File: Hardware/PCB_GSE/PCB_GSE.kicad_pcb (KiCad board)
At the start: 2 copper layers, 139 parts, among them J1 Conn_01x06_Pin, J2 Vin_XT30PW-F, J3 Screw_Terminal_01x06, J4 GT17HN-4DP-2H(D)(56), J5 Conn_02x10_Top_Bottom, J6 Conn_01x02, J7 Screw_Terminal_01x04, J8 Screw_Terminal_01x04, U1 STM32F103CBT6, U10 INA125UA/2K5, U11 MAX6612MXK, U2 LM2673SX-12_NOPB, U3 MPQ9843GLE-5-AEC1-Z, U4 TLV75733PDBVR, U5 SI5442DU-T1-GE3, U6 SI5442DU-T1-GE3, U7 SI5442DU-T1-GE3, U8 ISOW1044, U9 INA125UA/2K5

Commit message: feat: add 8MHz crystal, fix extended ios, fix pinout with HSE, update smt32 project, begin layout edge
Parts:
- added C54: 22pF, Capacitor_SMD:C_0805_2012Metric, F.Cu at (141.7, 49.2)
- added C55: 22pF, Capacitor_SMD:C_0805_2012Metric, F.Cu at (141.7, 52.2)
- added R42: 10R, Resistor_SMD:R_0805_2012Metric, F.Cu at (146.2, 49.1)
- added XTAL-1: 830050510, PCB_GSE:830050510, F.Cu at (147.6, 44.4)
- J5: value Conn_02x10_Top_Bottom -> Conn_02x09_Top_Bottom; footprint Connector_PinHeader_2.54mm:PinHeader_2x10_P2.54mm_Vertical -> Connector_PinHeader_2.54mm:PinHeader_2x09_P2.54mm_Vertical
- moved C13 130.5 mm to (211.3, 34.4)
- moved C20 130.5 mm to (211.3, 41.9)
- moved C22 130.5 mm to (217.4, 30.8)
- moved C23 130.5 mm to (269.4, 23.3)
- moved C26 130.5 mm to (211.3, 38.1)
- moved C28 130.5 mm to (269.4, 29.3)
- moved C31 130.5 mm to (269.4, 32.3)
- moved C33 130.5 mm to (218.1, 63.7)
- moved C39 130.5 mm to (257.5, 54.4)
- moved C40 130.5 mm to (257.5, 57.4)
- moved C42 130.5 mm to (257.5, 60.4)
- moved C44 130.5 mm to (261.9, 54.4)
- moved C46 130.5 mm to (261.9, 57.4)
- moved C47 130.5 mm to (261.9, 60.4)
- moved C48 130.5 mm to (349.9, 54.2)
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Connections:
- J5 pad 10: LC_IN- -> 12V_Main
- J5 pad 11: 12V_Main -> EXTEND_IO6
- J5 pad 18: EXTEND_IO13 -> LC_IN-
- J5 pad 8: EXTEND_IO6 -> LC_IN-
- R4 pad 2: Net-(U1-PD0) -> Net-(U1-PC14)
- R5 pad 2: Net-(U1-PD1) -> Net-(U1-PC15)
- U1 pad 18: EXTEND_IO3 -> EXTEND_IO1
- U1 pad 19: EXTEND_IO4 -> EXTEND_IO2
- U1 pad 20: EXTEND_IO5 -> EXTEND_IO3
- U1 pad 25: EXTEND_IO6 -> EXTEND_IO4
- U1 pad 26: EXTEND_IO7 -> EXTEND_IO5
- U1 pad 27: EXTEND_IO8 -> EXTEND_IO6
- U1 pad 28: EXTEND_IO9 -> EXTEND_IO7
- U1 pad 29: EXTEND_IO10 -> EXTEND_IO8
- U1 pad 3: EXTEND_IO1 -> Net-(U1-PC14)
- U1 pad 30: EXTEND_IO11 -> EXTEND_IO9
- U1 pad 38: EXTEND_IO12 -> EXTEND_IO10
- U1 pad 4: EXTEND_IO2 -> Net-(U1-PC15)
- U1 pad 40: EXTEND_IO13 -> EXTEND_IO11
- U1 pad 41: EXTEND_IO14 -> EXTEND_IO12
- U1 pad 5: Net-(U1-PD0) -> OSC_IN
- U1 pad 6: Net-(U1-PD1) -> OSC_OUT
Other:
- board outline added: 76.2 x 101.6 mm

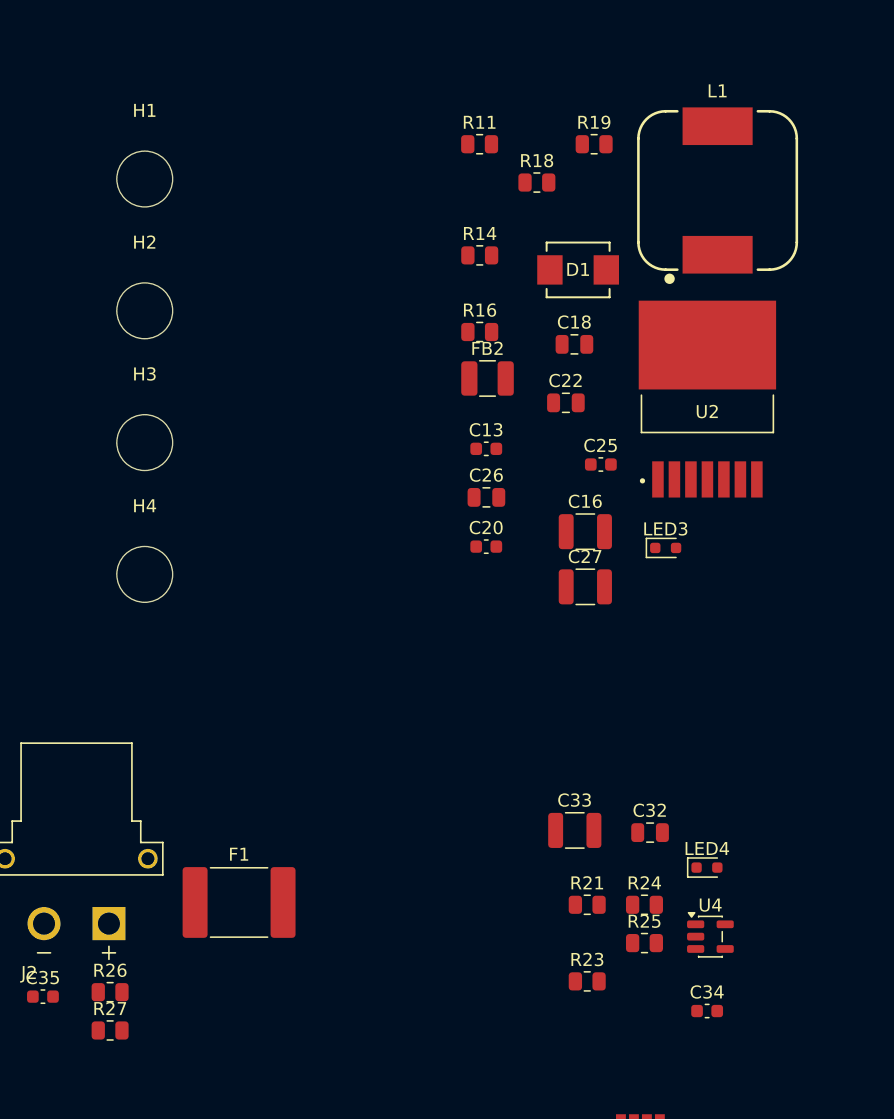
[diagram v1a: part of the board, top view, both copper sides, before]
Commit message: fix(GSE & Moteur): change Vin adc divider
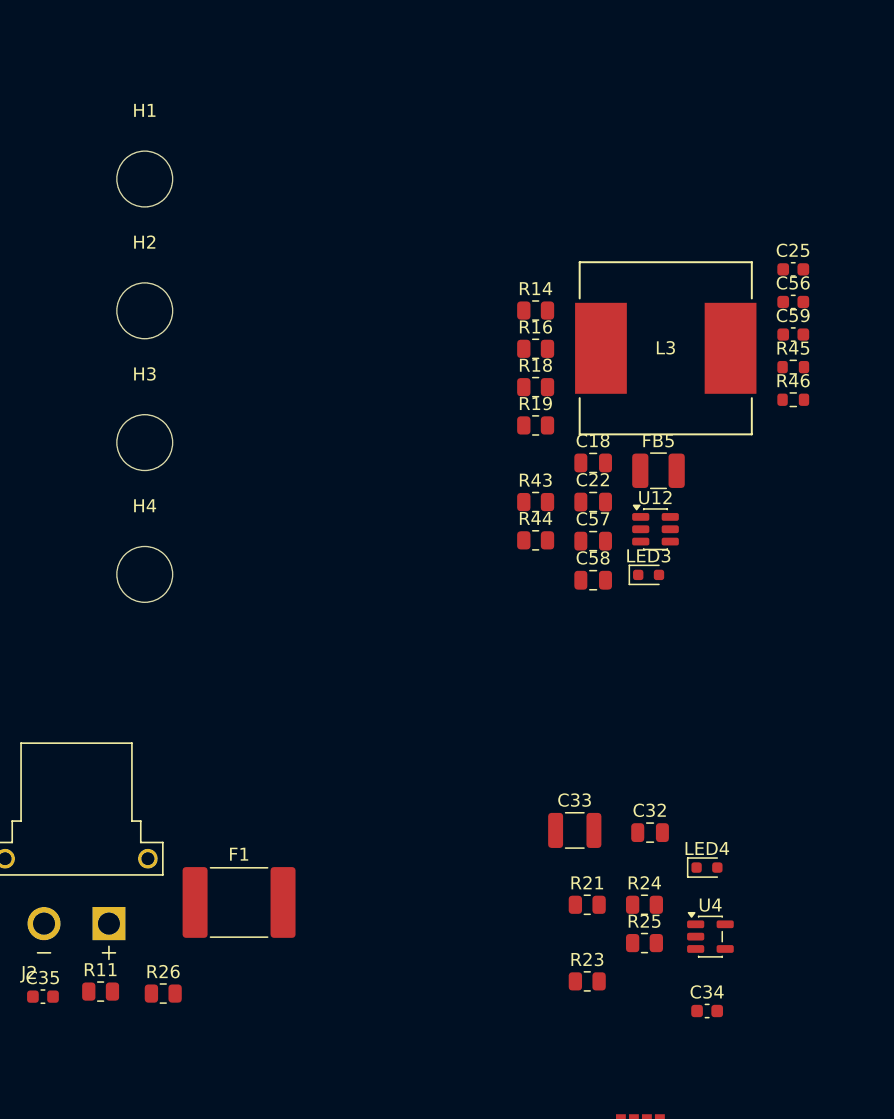
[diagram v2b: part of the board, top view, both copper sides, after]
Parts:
- removed C13, C20: 100nF, Capacitor_SMD:C_0603_1608Metric
- removed C16, C27: 100uF, Capacitor_SMD:C_1210_3225Metric
- removed C26: 10nF, Capacitor_SMD:C_0805_2012Metric
- removed D1: MBRS540T3G, pcb_moteur:DIODE_SMB_2L_ONS
- removed FB2: 600R, Inductor_SMD:L_1210_3225Metric
- removed L1: 33uH, pcb_moteur:WE-PD_1245
- removed R27: 390k 1%, Resistor_SMD:R_0805_2012Metric
- removed U2: LM2673SX-12_NOPB, PCB_GSE:LM2673SX-12_NOPB
- added C56: 100nF, Capacitor_SMD:C_0603_1608Metric, F.Cu at (234.9, 23.0)
- added C57: 22uF, Capacitor_SMD:C_0805_2012Metric, F.Cu at (219.5, 41.5)
- added C58: 22uF, Capacitor_SMD:C_0805_2012Metric, F.Cu at (219.5, 44.5)
- added C59: 100pf, Capacitor_SMD:C_0603_1608Metric, F.Cu at (234.9, 25.5)
- added FB5: 600R, Inductor_SMD:L_1210_3225Metric, F.Cu at (224.5, 36.0)
- added L3: SRR1208-150ML, PCB_GSE:IND_BOURNS_SRR1208, F.Cu at (225.1, 26.6)
- added R43: 1.5k, Resistor_SMD:R_0805_2012Metric, F.Cu at (215.1, 38.4)
- added R44: 100k 1%, Resistor_SMD:R_0805_2012Metric, F.Cu at (215.1, 41.4)
- added R45: 5k23 1%, Resistor_SMD:R_0603_1608Metric, F.Cu at (234.9, 28.1)
- added R46: 49.9k 1%, Resistor_SMD:R_0603_1608Metric, F.Cu at (234.9, 30.6)
- added U12: TPS54302, Package_TO_SOT_SMD:SOT-23-6, F.Cu at (224.3, 40.5)
- moved R11 71.5 mm to (181.6, 76.1)
- moved R19 22.1 mm to (215.1, 32.5)
- moved C25 21.1 mm to (234.9, 20.5)
- moved R18 15.8 mm to (215.1, 29.6)
- moved C18 9.25 mm to (219.5, 35.4)
- moved C22 7.93 mm to (219.5, 38.4)
- moved R14 6.05 mm to (215.1, 23.7)
- moved R16 4.50 mm to (215.1, 26.6)
- moved R26 4.09 mm to (186.4, 76.3)
- moved LED3 2.46 mm to (223.8, 44.1)
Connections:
- R11 pad 1: LC_IN- -> Vin_An
- R11 pad 2: Net-(U2-CURRENT_ADJ) -> LC_IN-
- R26 pad 1: LC_IN- -> VIN_Filtered

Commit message: wip : subsystems layout
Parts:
- removed D6: BAT54S, Package_TO_SOT_SMD:SOT-23
- removed FB5: 600R, Inductor_SMD:L_1210_3225Metric
- removed L3: SRR1208-150ML, PCB_GSE:IND_BOURNS_SRR1208
- removed U12: TPS54302, Package_TO_SOT_SMD:SOT-23-6
- added C13: 10uF, Capacitor_SMD:C_0805_2012Metric, F.Cu at (86.5, -15.5)
- added C16: 100nF, Capacitor_SMD:C_0603_1608Metric, F.Cu at (190.4, -40.3)
- added C20: 100nF, Capacitor_SMD:C_0603_1608Metric, F.Cu at (133.6, -41.6)
- added C26: 100nF, Capacitor_SMD:C_0603_1608Metric, F.Cu at (214.3, -35.5)
- added C27: 100nF, Capacitor_SMD:C_0603_1608Metric, F.Cu at (135.3, -38.7)
- added C60: 100nF, Capacitor_SMD:C_0603_1608Metric, F.Cu at (326.2, 78.9)
- added C61: 10nF, Capacitor_SMD:C_0805_2012Metric, F.Cu at (170.2, 29.2)
- added C62: 100nF, Capacitor_SMD:C_0603_1608Metric, F.Cu at (175.5, 29.2)
- added D1: MBRS540T3G, pcb_moteur:DIODE_SMB_2L_ONS, F.Cu at (275.8, 84.0)
- added FB2: 600R, Inductor_SMD:L_1210_3225Metric, F.Cu at (122.9, -29.2)
- added L1: 3.3uH, PCB_GSE:MPL-AL6050-3R3, F.Cu at (140.3, -48.4)
- added R27: 10k, Resistor_SMD:R_0805_2012Metric, F.Cu at (140.9, -23.4)
- added R47: 1k, Resistor_SMD:R_0805_2012Metric, F.Cu at (340.5, 96.8)
- added R48: 1.5k, Resistor_SMD:R_0805_2012Metric, F.Cu at (328.9, 101.1)
- added R49: 1.5k, Resistor_SMD:R_0805_2012Metric, F.Cu at (329.3, 78.1)
- added U2: MPQ9843GLE-5-AEC1-Z, pcb_moteur:MPQ9843GLE_5_AEC1_Z, F.Cu at (194.2, -41.6)
- C10: value 100uF -> 22pF; footprint PCB_GSE:U2-K_NCH -> Capacitor_SMD:C_0805_2012Metric
- C11, C44: value 10uF -> 100nF; footprint Capacitor_SMD:C_0805_2012Metric -> Capacitor_SMD:C_0603_1608Metric
- C12: value 100nF -> 100uF; footprint Capacitor_SMD:C_0603_1608Metric -> PCB_GSE:U2-K_NCH
- C15, C19, C57, C58: value 22uF -> 100nF; footprint Capacitor_SMD:C_0805_2012Metric -> Capacitor_SMD:C_0603_1608Metric
- C2: value 10uF -> 22pF
- C24, C25, C35: value 100nF -> 22uF; footprint Capacitor_SMD:C_0603_1608Metric -> Capacitor_SMD:C_0805_2012Metric
- C28, C36: value 10uF -> 1uF
- C30, C51, C56, C6, C8: value 100nF -> 10nF; footprint Capacitor_SMD:C_0603_1608Metric -> Capacitor_SMD:C_0805_2012Metric
- C31, C40: value 1uF -> 100nF; footprint Capacitor_SMD:C_0805_2012Metric -> Capacitor_SMD:C_0603_1608Metric
- C33: value 100uF -> 100nF; footprint Capacitor_SMD:C_1210_3225Metric -> Capacitor_SMD:C_0603_1608Metric
- C37, C38, C39: value 10uF -> 22uF
- C4, C41, C45, C48, C53: value 100nF -> 10uF; footprint Capacitor_SMD:C_0603_1608Metric -> Capacitor_SMD:C_0805_2012Metric
- C42: value 10nF -> 100uF; footprint Capacitor_SMD:C_0805_2012Metric -> Capacitor_SMD:C_1210_3225Metric
- C46: value 1uF -> 10uF
- C47: value 10nF -> 10uF
- C49: value 100nF -> 1uF; footprint Capacitor_SMD:C_0603_1608Metric -> Capacitor_SMD:C_0805_2012Metric
- C5, C52, C7: value 10nF -> 100nF; footprint Capacitor_SMD:C_0805_2012Metric -> Capacitor_SMD:C_0603_1608Metric
- C54: value 22pF -> 100nF; footprint Capacitor_SMD:C_0805_2012Metric -> Capacitor_SMD:C_0603_1608Metric
- C55: value 22pF -> 1uF
- C59: value 100pf -> 100nF
- D4: value MBRS540T3G -> BAT54S; footprint pcb_moteur:DIODE_SMB_2L_ONS -> Package_TO_SOT_SMD:SOT-23
- J5: value Conn_02x09_Top_Bottom -> Conn_02x07_Odd_Even; footprint Connector_PinHeader_2.54mm:PinHeader_2x09_P2.54mm_Vertical -> Connector_PinHeader_2.54mm:PinHeader_2x07_P2.54mm_Vertical
- R10: value 10k -> 22R; footprint Resistor_SMD:R_0805_2012Metric -> Resistor_SMD:R_0603_1608Metric
- R11: value 12k 1% -> 1.5k
- R12, R16, R44: value 100k 1% -> 10k
- R13, R29: value 10k -> 10R
- R17: value 1.5k -> 100k 1%
- R19, R32: value 10k -> 100k 1%
- R20: value 191k 1% -> 100k 1%
- R21: value 12k 1% -> 21.5k
- R22: value 10R -> 1.5k
- R23: value 100k 1% -> 806k
- R24: value 1.5k -> 402k
- R25: value 1.5k -> 18.7k
- R26: value 100k 1% -> 191k 1%
- R30, R31: value 200R -> 12k 1%
- R33: value 200R -> 100k 1%
- R34, R35: value 60R -> 1.5k
- R39: value 1k -> 200R
- R4, R5: value 22R -> 10k; footprint Resistor_SMD:R_0603_1608Metric -> Resistor_SMD:R_0805_2012Metric
- R40: value 1.5k -> 10k
- R41: value 1.5k -> 200R
- R42: value 10R -> 59R
- R43: value 1.5k -> 59R
- R45: value 5k23 1% -> 10k; footprint Resistor_SMD:R_0603_1608Metric -> Resistor_SMD:R_0805_2012Metric
- R46: value 49.9k 1% -> 200R; footprint Resistor_SMD:R_0603_1608Metric -> Resistor_SMD:R_0805_2012Metric
- R9: value 1.5k -> 22R; footprint Resistor_SMD:R_0805_2012Metric -> Resistor_SMD:R_0603_1608Metric
- U3: value MPQ9843GLE-5-AEC1-Z -> MP28167GQ-B-P; footprint pcb_moteur:MPQ9843GLE_5_AEC1_Z -> PCB_GSE:QFN-16_MP28167_MNP
- moved R32 252.2 mm to (65.3, -28.5)
- moved R30 248.9 mm to (65.3, -30.6), turned to 180 degrees
- moved C43 221.3 mm to (65.3, -32.4), turned to 180 degrees
- moved R13 204.0 mm to (55.8, 61.5)
- moved R12 195.5 mm to (63.3, 53.0)
- moved C37 192.8 mm to (149.4, -41.6), turned to -90 degrees
- moved C38 186.1 mm to (147.3, -41.6), turned to -90 degrees
- moved C15 183.9 mm to (86.5, -18.2)
- moved R28 171.8 mm to (140.9, -21.3)
- moved F1 156.8 mm to (60.7, -16.1), turned to 180 degrees
- moved C29 156.4 mm to (137.6, -44.1), turned to 180 degrees
- moved C17 156.1 mm to (135.2, -41.6), turned to -90 degrees
- moved J2 154.2 mm to (47.6, -13.6), turned to 90 degrees
- moved C23 152.2 mm to (131.7, -41.6), turned to -90 degrees
- moved C30 151.2 mm to (140.3, -35.3), turned to 90 degrees
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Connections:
- C1 pad 2: LC_IN- -> GND
- C10 pad 1: VIN_Filtered -> GND
- C10 pad 2: LC_IN- -> Net-(C10-Pad2)
- C11 pad 1: VIN_Filtered -> GND
- C11 pad 2: LC_IN- -> 3V_Main
- C12 pad 2: LC_IN- -> GND
- C14 pad 1: Net-(U3-EN) -> 12V_An
- C14 pad 2: LC_IN- -> GND
- C15 pad 1: 5V_Main -> VIN_Filtered
- C15 pad 2: LC_IN- -> GND
- C17 pad 1: Net-(U3-EN) -> Net-(U3-IN)
- C17 pad 2: LC_IN- -> GND
- C18 pad 1: 12V_Main -> 5V_Main
- C18 pad 2: LC_IN- -> GND
- C19 pad 1: 5V_Main -> Net-(U2-EN)
- C19 pad 2: LC_IN- -> GND
- C2 pad 1: LC_IN- -> GND
- C2 pad 2: 3V_Main -> OSC_IN
- C21 pad 1: Net-(U3-EN) -> 5V_Main
- C21 pad 2: LC_IN- -> GND
- C22 pad 1: 12V_Main -> Net-(U2-EN)
- C22 pad 2: LC_IN- -> GND
- C23 pad 1: Net-(U3-EN) -> Net-(U3-IN)
- C23 pad 2: LC_IN- -> GND
- C24 pad 1: 5V_An -> Net-(U2-EN)
- C24 pad 2: LC_IN- -> GND
- C25 pad 1: 12V_An -> Net-(U3-IN)
- C25 pad 2: LC_IN- -> GND
- C28 pad 1: Net-(U3-SS) -> Net-(U3-VCC)
- C28 pad 2: LC_IN- -> GND
- C29 pad 1: Net-(U3-BST) -> Net-(U3-BST1)
- C29 pad 2: Net-(C29-Pad2) -> Net-(U3-SW1)
- C3 pad 1: LC_IN- -> GND
- C3 pad 2: +3.3VA -> 3V_Main
- C30 pad 1: Net-(U3-BIAS) -> GND
- C30 pad 2: LC_IN- -> Net-(U3-OC)
- C31 pad 1: Net-(U3-VCC) -> Net-(U3-BST2)
- C31 pad 2: LC_IN- -> Net-(U3-SW2)
- C32 pad 1: 5V_Main -> Net-(U2-SS)
- C32 pad 2: LC_IN- -> GND
- C33 pad 1: 3V_Main -> Net-(U2-BST)
- C33 pad 2: LC_IN- -> Net-(C33-Pad2)
- C34 pad 1: 3V3_An -> Net-(U2-BIAS)
- C34 pad 2: LC_IN- -> GND
- C35 pad 1: Vin_An -> Vin_Valve
- C35 pad 2: LC_IN- -> GND
- C36 pad 1: 12V_Main -> Net-(U2-VCC)
- C36 pad 2: LC_IN- -> GND
- C37 pad 1: 12V_Main -> Vin_Valve
- C37 pad 2: LC_IN- -> GND
- C38 pad 1: 12V_Main -> Vin_Valve
- C38 pad 2: LC_IN- -> GND
- C39 pad 1: 3V_Main -> Vin_Valve
- C39 pad 2: LC_IN- -> GND
- C4 pad 1: LC_IN- -> GND
- C4 pad 2: 3V_Main -> +3.3VA
- C40 pad 1: 3V_Main -> Vin_Valve
- C40 pad 2: LC_IN- -> GND
- C41 pad 1: 3V_Main -> 5V_Main
- C41 pad 2: LC_IN- -> GND
- C42 pad 2: LC_IN- -> GND
- C43 pad 1: +5Viso -> Vin_An
- C43 pad 2: GND_iso -> GND
- C44 pad 1: +5VAiso -> 3V3_An
- C44 pad 2: GND_iso -> GND
- C45 pad 1: Net-(C45-Pad1) -> Vin_Valve
- C45 pad 2: GND_iso -> GND
- C46 pad 1: +5VAiso -> Vin_Valve
- C46 pad 2: GND_iso -> GND
- C47 pad 1: +5VAiso -> Vin_Valve
- C47 pad 2: GND_iso -> GND
- C48 pad 1: VIN_Filtered -> 3V_Main
- C48 pad 2: LC_IN- -> GND
- C49 pad 1: VIN_Filtered -> 3V_Main
- C49 pad 2: LC_IN- -> GND
- C5 pad 1: LC_IN- -> GND
- C5 pad 2: +3.3VA -> 3V_Main
- C50 pad 1: Pressure_An -> 3V_Main
- C50 pad 2: LC_IN- -> GND
- C51 pad 1: LCell_An -> 3V_Main
- C51 pad 2: LC_IN- -> GND
- C52 pad 1: Temp_An -> +5Viso
- C52 pad 2: LC_IN- -> GND_iso
- C53 pad 1: 3V_Main -> +5VAiso
- C53 pad 2: LC_IN- -> GND_iso
- C54 pad 1: LC_IN- -> Net-(C54-Pad1)
- C54 pad 2: Net-(C54-Pad2) -> GND_iso
- C55 pad 1: LC_IN- -> +5VAiso
- C55 pad 2: OSC_IN -> GND_iso
- C56 pad 1: Net-(U12-BOOT) -> +5VAiso
- C56 pad 2: Net-(U12-SW) -> GND_iso
- C57 pad 1: 12V_Main -> VIN_Filtered
- C57 pad 2: LC_IN- -> GND
- C58 pad 1: 12V_Main -> VIN_Filtered
- C58 pad 2: LC_IN- -> GND
- C59 pad 1: Net-(U12-FB) -> Pressure_An
- C59 pad 2: Net-(C59-Pad2) -> GND
- C6 pad 1: LC_IN- -> GND
- C6 pad 2: 3V_Main -> +3.3VA
- C7 pad 1: LC_IN- -> GND
- C8 pad 1: LC_IN- -> GND
- C9 pad 1: LC_IN- -> GND
- D2 pad 1: 12V_Main -> Vin_Valve
- D2 pad 2: Valve1- -> Valve3-
- D3 pad 1: 12V_Main -> Vin_Valve
- D3 pad 2: Valve3- -> Valve2-
- D4 pad 1: 12V_Main -> GND
- D4 pad 2: Valve2- -> +3.3VA
- D5 pad 1: LC_IN- -> GND
- FB3 pad 2: Net-(U3-EN) -> Net-(U2-EN)
- J1 pad 5: LC_IN- -> GND
- J2 pad N: LC_IN- -> GND
- J3 pad 1: 12V_Main -> Vin_Valve
- J3 pad 3: 12V_Main -> Vin_Valve
- J3 pad 5: 12V_Main -> Vin_Valve
- J4 pad 4: LC_IN- -> GND
- J4 pad 5: LC_IN- -> GND
- J5 pad 1: 5V_Main -> Vin_Valve
- J5 pad 10: 12V_Main -> EXTEND_IO10
- J5 pad 11: EXTEND_IO6 -> EXTEND_IO7
- J5 pad 12: EXTEND_IO7 -> EXTEND_IO11
- J5 pad 13: EXTEND_IO8 -> GND
- J5 pad 14: EXTEND_IO9 -> EXTEND_IO12
- J5 pad 3: EXTEND_IO1 -> EXTEND_IO2
- J5 pad 4: EXTEND_IO2 -> 5V_Main
- J5 pad 6: EXTEND_IO4 -> EXTEND_IO8
- J5 pad 8: LC_IN- -> EXTEND_IO9
- J5 pad 9: LC_IN- -> EXTEND_IO6
- J7 pad 2: LC_IN- -> GND
- J8 pad 2: LC_IN- -> GND
- L2 pad 2: Net-(C29-Pad2) -> Net-(C33-Pad2)
- LED2 pad 1: LC_IN- -> GND
- LED3 pad 1: LC_IN- -> GND
- LED4 pad 1: LC_IN- -> GND
- R10 pad 1: LC_IN- -> ISO_CAN_TXD
- R10 pad 2: BOOT0 -> Net-(U1-PB9)
- R11 pad 1: Vin_An -> BOOT0
- R11 pad 2: LC_IN- -> Net-(JP1-B)
- R12 pad 1: 5V_An -> GND
- R12 pad 2: 5V_Main -> BOOT0
- R13 pad 1: 3V_Main -> Net-(C10-Pad2)
- R13 pad 2: Power_Good -> OSC_OUT
- R14 pad 1: 12V_An -> Vin_Valve
- R14 pad 2: 12V_Main -> 12V_An
- R15 pad 1: LC_IN- -> 12V_An
- R15 pad 2: 5V_An -> GND
- R16 pad 1: LC_IN- -> 3V_Main
- R16 pad 2: 12V_An -> Power_Good_12V
- R17 pad 1: Net-(LED2-A) -> 5V_An
- R18 pad 1: 12V_Main -> 3V_Main
- R18 pad 2: Net-(LED3-A) -> Power_Good_5V
- R19 pad 1: 12V_Main -> Net-(U3-IN)
- R19 pad 2: Net-(LED3-A) -> Net-(U3-EN)
- R20 pad 1: Net-(U3-FREQ) -> GND
- R20 pad 2: LC_IN- -> 5V_An
- R21 pad 1: 3V3_An -> Net-(U3-OC)
- R21 pad 2: 3V_Main -> GND
- R22 pad 1: 5V_Main -> Net-(LED2-A)
- R22 pad 2: Net-(U3-BIAS) -> 5V_Main
- R23 pad 1: LC_IN- -> Net-(U3-FB)
- R23 pad 2: 3V3_An -> Net-(R23-Pad2)
- R24 pad 1: Net-(LED4-A) -> Vin_Valve
- R24 pad 2: 3V_Main -> Net-(R23-Pad2)
- R25 pad 1: Net-(LED4-A) -> Net-(R23-Pad2)
- R25 pad 2: 3V_Main -> GND
- R26 pad 1: VIN_Filtered -> Net-(U2-FREQ)
- R26 pad 2: Vin_An -> GND
- R28 pad 1: Valve1_Open -> Vin_Valve
- R28 pad 2: LC_IN- -> Net-(LED3-A)
- R29 pad 1: Valve3_Open -> 5V_Main
- R29 pad 2: LC_IN- -> Net-(U2-BIAS)
- R3 pad 1: 3V_Main -> I2C2_SCL
- R3 pad 2: SYS_NRST -> 3V_Main
- R30 pad 1: Valve1_Open -> Vin_An
- R30 pad 2: Net-(U5-G) -> GND
- R31 pad 1: Valve3_Open -> 3V3_An
- R31 pad 2: Net-(U6-G) -> 3V_Main
- R32 pad 1: Valve2_Open -> VIN_Filtered
- R32 pad 2: LC_IN- -> Vin_An
- R33 pad 1: Valve2_Open -> GND
- R33 pad 2: Net-(U7-G) -> 3V3_An
- R34 pad 1: Net-(C45-Pad1) -> Net-(LED4-A)
- R34 pad 2: /Interfaces/CAN+ -> 3V_Main
- R35 pad 1: /Interfaces/CAN- -> Net-(LED4-A)
- R35 pad 2: Net-(C45-Pad1) -> 3V_Main
- R36 pad 1: LCell_Sleep -> Valve1_Open
- R36 pad 2: LC_IN- -> GND
- R37 pad 1: Pressure_Sleep -> Valve3_Open
- R37 pad 2: LC_IN- -> GND
- R38 pad 1: Net-(R38-Pad1) -> Valve1_Open
- R38 pad 2: Net-(R38-Pad2) -> Net-(U5-G)
- R39 pad 1: Net-(R39-Pad1) -> Valve3_Open
- R39 pad 2: Net-(R39-Pad2) -> Net-(U6-G)
- R4 pad 1: Pressure_Sleep -> I2C2_SDA
- R4 pad 2: Net-(U1-PC14) -> 3V_Main
- R40 pad 1: Net-(D5-COM) -> Valve2_Open
- R40 pad 2: Pressure_An -> GND
- R41 pad 1: Net-(D6-COM) -> Valve2_Open
- R41 pad 2: LCell_An -> Net-(U7-G)
- R42 pad 1: Net-(C54-Pad2) -> Net-(C54-Pad1)
- R42 pad 2: OSC_OUT -> /Interfaces/CAN+
- R43 pad 1: Net-(U12-EN) -> /Interfaces/CAN-
- R43 pad 2: Net-(U12-VIN) -> Net-(C54-Pad1)
- R44 pad 1: Net-(U12-FB) -> LCell_Sleep
- R44 pad 2: Net-(C59-Pad2) -> GND
- R45 pad 1: LC_IN- -> Pressure_Sleep
- R45 pad 2: Net-(U12-FB) -> GND
- R46 pad 1: Net-(C59-Pad2) -> Net-(R46-Pad1)
- R46 pad 2: 12V_Main -> Net-(R46-Pad2)
- R5 pad 1: LCell_Sleep -> 3V_Main
- R5 pad 2: Net-(U1-PC15) -> SYS_NRST
- R7 pad 1: RFD_USART1_TX -> Pressure_Sleep
- R7 pad 2: Net-(U1-PB6) -> Net-(U1-PC14)
- R8 pad 1: ISO_CAN_TXD -> LCell_Sleep
- R8 pad 2: Net-(U1-PB9) -> Net-(U1-PC15)
- R9 pad 1: BOOT0 -> RFD_USART1_TX
- R9 pad 2: Net-(JP1-B) -> Net-(U1-PB6)
- U1 pad 17: Power_Good -> Power_Good_5V
- U1 pad 18: EXTEND_IO1 -> CriticalLED_G
- U1 pad 19: EXTEND_IO2 -> CriticalLED_R
- U1 pad 21: CriticalLED_G -> I2C2_SCL
- U1 pad 22: CriticalLED_R -> I2C2_SDA
- U1 pad 23: LC_IN- -> GND
- U1 pad 25: EXTEND_IO4 -> Power_Good_12V
- U1 pad 35: LC_IN- -> GND
- U1 pad 47: LC_IN- -> GND
- U1 pad 8: LC_IN- -> GND
- U10 pad 10: Net-(D5-COM) -> Net-(D4-COM)
- U10 pad 11: Net-(D5-COM) -> Net-(D4-COM)
- U10 pad 12: LC_IN- -> GND
- U10 pad 3: LC_IN- -> GND
- U10 pad 5: LC_IN- -> GND
- U10 pad 8: Net-(R39-Pad2) -> Net-(R47-Pad2)
- U10 pad 9: Net-(R39-Pad1) -> Net-(R47-Pad1)
- U11 pad 1: LC_IN- -> GND
- U11 pad 2: LC_IN- -> GND
- U11 pad 5: LC_IN- -> GND
- U3 pad 1: LC_IN- -> Net-(U3-IN)
- U3 pad 10: Net-(C29-Pad2) -> GND
- U3 pad 11: Net-(U3-BST) -> GND
- U3 pad 12: Net-(U3-VCC) -> Vin_Valve
- U3 pad 13: LC_IN- -> Net-(U3-BST2)
- U3 pad 14: Net-(U3-SS) -> Net-(U3-SW2)
- U3 pad 15: 5V_Main -> Net-(U3-SW1)
- U3 pad 16: Net-(U3-FREQ) -> Net-(U3-BST1)
- U3 pad 2: Net-(U3-EN) -> GND
- U3 pad 3: unconnected-(U3-SW-Pad3) -> Net-(U3-EN)
- U3 pad 4: LC_IN- -> Power_Good_12V
- U3 pad 5: Net-(U3-EN) -> I2C2_SCL
- U3 pad 6: unconnected-(U3-SYNC-Pad6) -> I2C2_SDA
- U3 pad 7: Power_Good -> Net-(U3-OC)
- U3 pad 8: Net-(U3-BIAS) -> Net-(U3-FB)
- U3 pad 9: LC_IN- -> Net-(U3-VCC)
- U4 pad 2: LC_IN- -> GND
- U5 pad 5: LC_IN- -> GND
- U5 pad 9: LC_IN- -> GND
- U6 pad 5: LC_IN- -> GND
- U6 pad 9: LC_IN- -> GND
- U7 pad 5: LC_IN- -> GND
- U7 pad 9: LC_IN- -> GND
- U8 pad 10: LC_IN- -> GND
- U8 pad 4: LC_IN- -> GND
- U8 pad 6: LC_IN- -> GND
- U9 pad 10: Net-(D6-COM) -> Net-(D5-COM)
- U9 pad 11: Net-(D6-COM) -> Net-(D5-COM)
- U9 pad 12: LC_IN- -> GND
- U9 pad 3: LC_IN- -> GND
- U9 pad 5: LC_IN- -> GND
- U9 pad 8: Net-(R38-Pad2) -> Net-(R46-Pad2)
- U9 pad 9: Net-(R38-Pad1) -> Net-(R46-Pad1)
- XTAL-1 pad 2: Net-(C54-Pad2) -> Net-(C10-Pad2)
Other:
- board outline removed

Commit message: wip(gse): edge
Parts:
- moved C12 338.4 mm to (412.5, -56.9)
- moved C13 338.4 mm to (422.5, -56.6)
- moved C15 338.4 mm to (422.5, -59.2)
- moved C43 338.4 mm to (401.2, -73.5)
- moved J2 338.4 mm to (383.5, -54.7)
- moved R1 338.4 mm to (397.8, 49.6)
- moved R30 338.4 mm to (401.2, -71.6)
- moved F1 338.4 mm to (396.6, -57.1)
- moved J1 338.4 mm to (364.3, 27.6)
- moved LED1 338.4 mm to (393.6, 49.4)
- moved R2 338.4 mm to (390.0, 49.5)
- moved R32 338.4 mm to (401.2, -69.6)
- moved TP1 338.4 mm to (354.7, 32.6)
- moved TP2 338.4 mm to (354.7, 35.6)
- moved TP3 338.4 mm to (354.7, 38.7)
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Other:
- board outline added: 76.2 x 127 mm

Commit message: wip(gse): begin layout
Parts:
- moved C15 430.7 mm to (24.8, 106.2)
- moved C13 430.2 mm to (25.0, 108.1)
- moved R30 426.4 mm to (13.5, 105.9)
- moved C43 426.3 mm to (15.3, 107.7)
- moved R32 422.4 mm to (17.0, 105.9), turned to 180 degrees
- moved C12 417.1 mm to (26.7, 101.8)
- moved F1 413.8 mm to (14.5, 101.7)
- moved J2 412.4 mm to (2.92, 104.1)
- moved J8 356.2 mm to (4.62, 46.7), turned to -90 degrees
- moved J7 354.8 mm to (4.60, 30.1), turned to -90 degrees
- moved LED1 343.1 mm to (58.2, 121.7)
- moved R1 343.1 mm to (62.4, 121.9)
- moved R2 343.1 mm to (54.6, 121.8)
- moved C58 340.8 mm to (9.51, 47.0), turned to -90 degrees
- moved C57 339.7 mm to (9.87, 30.5), turned to -90 degrees
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
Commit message: wip : finished layout and routing of powersupplys
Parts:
- moved J3 183.3 mm to (185.7, 98.3), turned to 90 degrees
- moved J5 178.1 mm to (240.3, 50.3), turned to 0 degrees
- moved D1 171.1 mm to (179.5, 98.9), turned to 90 degrees
- moved D3 169.6 mm to (179.5, 91.8), turned to 90 degrees
- moved D2 169.2 mm to (179.5, 84.7), turned to 90 degrees
- moved C45 163.2 mm to (175.1, 100.9), turned to 180 degrees
- moved U5 162.8 mm to (175.5, 97.8), turned to 0 degrees
- moved U7 161.4 mm to (175.5, 90.7), turned to 0 degrees
- moved U6 161.3 mm to (175.5, 83.6), turned to 0 degrees
- moved C47 161.0 mm to (175.0, 93.8), turned to 180 degrees
- moved C46 160.5 mm to (175.1, 86.7), turned to 180 degrees
- moved R38 158.1 mm to (173.1, 97.8), turned to -90 degrees
- moved R41 156.6 mm to (173.1, 90.7), turned to -90 degrees
- moved R39 156.5 mm to (173.1, 83.6), turned to -90 degrees
- moved R36 154.2 mm to (171.1, 97.8), turned to -90 degrees
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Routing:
- net 5V_Main: track 0.00 -> 35.0 mm, vias 0 -> 4
- net Net-(U2-EN): track 0.00 -> 9.49 mm, vias 0 -> 2
- net Net-(U2-BIAS): track 0.00 -> 8.63 mm
- net Net-(U3-EN): track 0.00 -> 6.46 mm
- net Net-(U3-OC): track 0.00 -> 5.83 mm
- net Power_Good_12V: track 0.00 -> 5.51 mm
- net Net-(U2-VCC): track 0.00 -> 5.01 mm
- net GND: track 0.00 -> 4.86 mm, vias 0 -> 102
- net Net-(U3-FB): track 0.00 -> 4.56 mm
- net Net-(R23-Pad2): track 0.00 -> 4.08 mm
- net 12V_An: track 0.00 -> 3.88 mm
- net Net-(U2-SS): track 0.00 -> 3.39 mm
- net Power_Good_5V: track 0.00 -> 3.20 mm, vias 0 -> 1
- net Net-(U2-FREQ): track 0.00 -> 3.10 mm
- net Net-(U3-VCC): track 0.00 -> 3.04 mm
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- added copper zone on F.Cu, net 5V_Main
- added copper zone on F.Cu, net GND
- added copper zone on F.Cu, net Net-(C33-Pad2)
- added copper zone on F.Cu, net Net-(U2-EN)
- added copper zone on F.Cu, net Net-(U3-IN)
- added copper zone on F.Cu, net Net-(U3-SW1)
- added copper zone on F.Cu, net Net-(U3-SW2)
- added copper zone on F.Cu, net Vin_Valve
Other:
- board size 76.2 x 127 mm -> 82.4 x 127 mm
- copper layers 2 -> 4

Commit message: wip : routing local circuits and power planes
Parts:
- removed J5: Conn_02x07_Odd_Even, Connector_PinHeader_2.54mm:PinHeader_2x07_P2.54mm_Vertical
- removed R6: 22R, Resistor_SMD:R_0603_1608Metric
- moved H1 75.7 mm to (181.8, 59.5)
- moved H2 67.6 mm to (120.5, 60.5)
- moved J6 36.7 mm to (150.8, 56.4), turned to 180 degrees
- moved LED1 36.0 mm to (181.1, 71.0)
- moved R1 36.0 mm to (185.3, 71.1)
- moved R2 36.0 mm to (177.4, 71.1)
- moved C56 29.2 mm to (160.0, 68.0), turned to 0 degrees
- moved C52 28.1 mm to (157.5, 62.2), turned to 90 degrees
- moved C53 28.0 mm to (159.5, 62.0), turned to 90 degrees
- moved C55 28.0 mm to (161.6, 62.0)
- moved FB4 26.0 mm to (158.6, 64.7)
- moved R42 26.0 mm to (151.4, 65.1)
- moved R43 25.1 mm to (152.3, 67.3)
- moved C45 24.2 mm to (184.6, 78.7), turned to 90 degrees
- moved C49 24.1 mm to (144.2, 79.0)
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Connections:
- U1 pad 2: Net-(U1-PC13) -> unconnected-(U1-PC13-Pad2)
- U8 pad 14: ISO_CAN_OUT -> unconnected-(U8-OUT-Pad14)
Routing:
- net VIN_Filtered: track 0.00 -> 71.4 mm
- net GND: track 4.86 -> 59.6 mm, vias 102 -> 176
- net Vin_Valve: track 0.00 -> 36.9 mm, vias 0 -> 2
- net +5Viso: track 0.00 -> 20.7 mm
- net GND_iso: track 0.00 -> 18.7 mm, vias 0 -> 12
- net 3V_Main: track 0.00 -> 18.0 mm
- net OSC_IN: track 0.00 -> 17.5 mm
- net LC_IN+: track 0.00 -> 14.2 mm
- net P_IN+: track 0.00 -> 14.0 mm
- net Net-(D5-COM): track 0.00 -> 12.6 mm
- net Valve3-: track 0.00 -> 12.4 mm
- net SYS_NRST: track 0.00 -> 12.1 mm
- net BOOT0: track 0.00 -> 11.8 mm
- net Valve1-: track 0.00 -> 11.7 mm
- net Valve2-: track 0.00 -> 11.6 mm
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- added copper zone on In1.Cu, net GND
- added copper zone on In1.Cu, net GND_iso
- added copper zone on F.Cu, net Net-(F1-Pad2)
- added copper zone on F.Cu, net VIN_Filtered
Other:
- board size 82.4 x 127 mm -> 74 x 95.6 mm
